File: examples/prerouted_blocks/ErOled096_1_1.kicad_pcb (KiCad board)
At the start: 2 copper layers, 9 parts

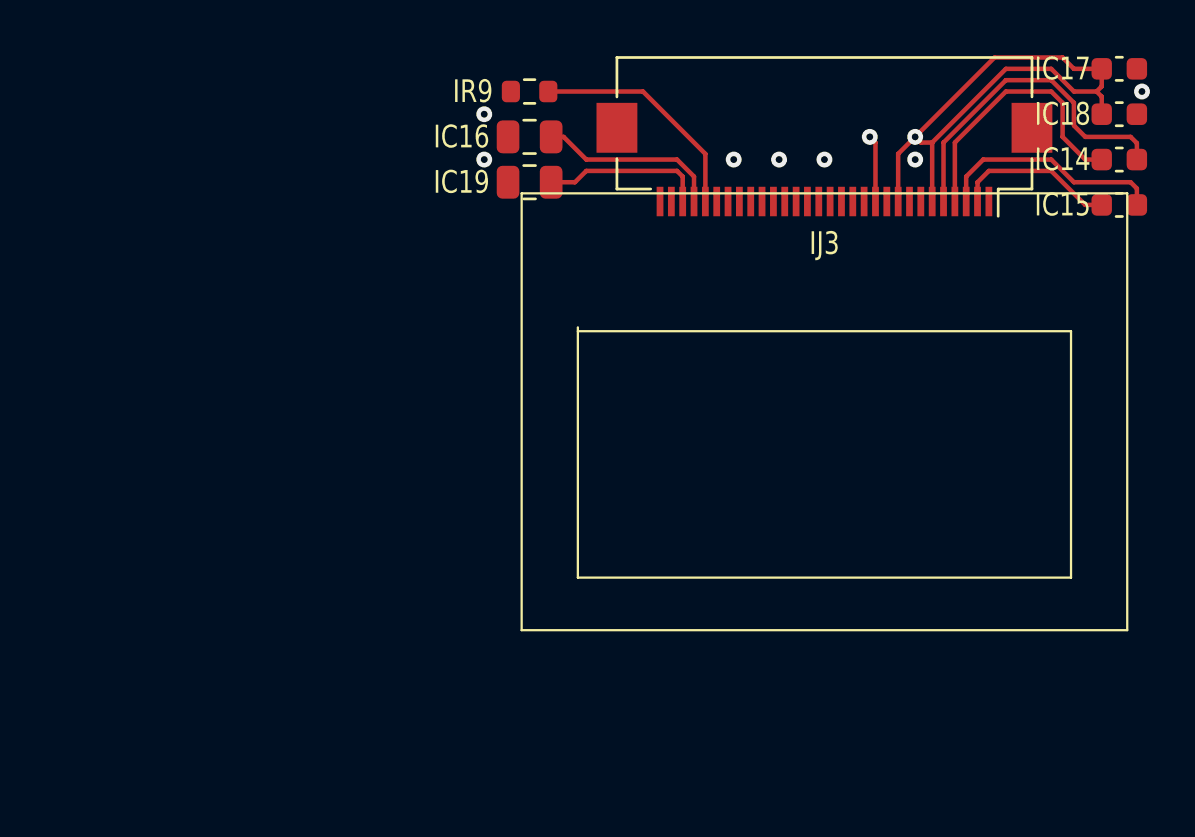
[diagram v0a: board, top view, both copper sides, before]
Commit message: Pcbbot (#314)
Robot driver that uses a ESP32 w/ camera and has student-proofing
  Key features:
  - USB-C receptacle for power input and battery charging.
- LiPo battery connector with voltage regulation and protection
circuits.
- Power management with priority power selection, fuse protection, and
gate control.
  - 3.3V voltage regulation for the main logic level power supply.
  - Integrated battery charging circuit with status indication.
  - I2C communication interface with pull-up resistors and test points.
  - Time-of-flight (ToF) sensor array for distance measurement.
- Inertial Measurement Unit (IMU) and magnetometer for orientation
sensing.
  - IO expander for additional GPIOs and a thru-hole RGB LED indicator.
  - OLED display
  - PWM Servo motor
  - Neopixel LED array for RGB lighting
  - Camera module with voltage regulation for image capture.
  - Digital switch for power control.
  - Keyboard mechanical switch with RGB LED
  - Ducky touch button
  
  Known issues:
  - Charging ic is not reverse protected
- MCU does not get turned off with the gate when powered by the USB and
battery, though the vbatt line turns off. (by design)

---------

Co-authored-by: Richard Lin <richard.lin@berkeley.edu>
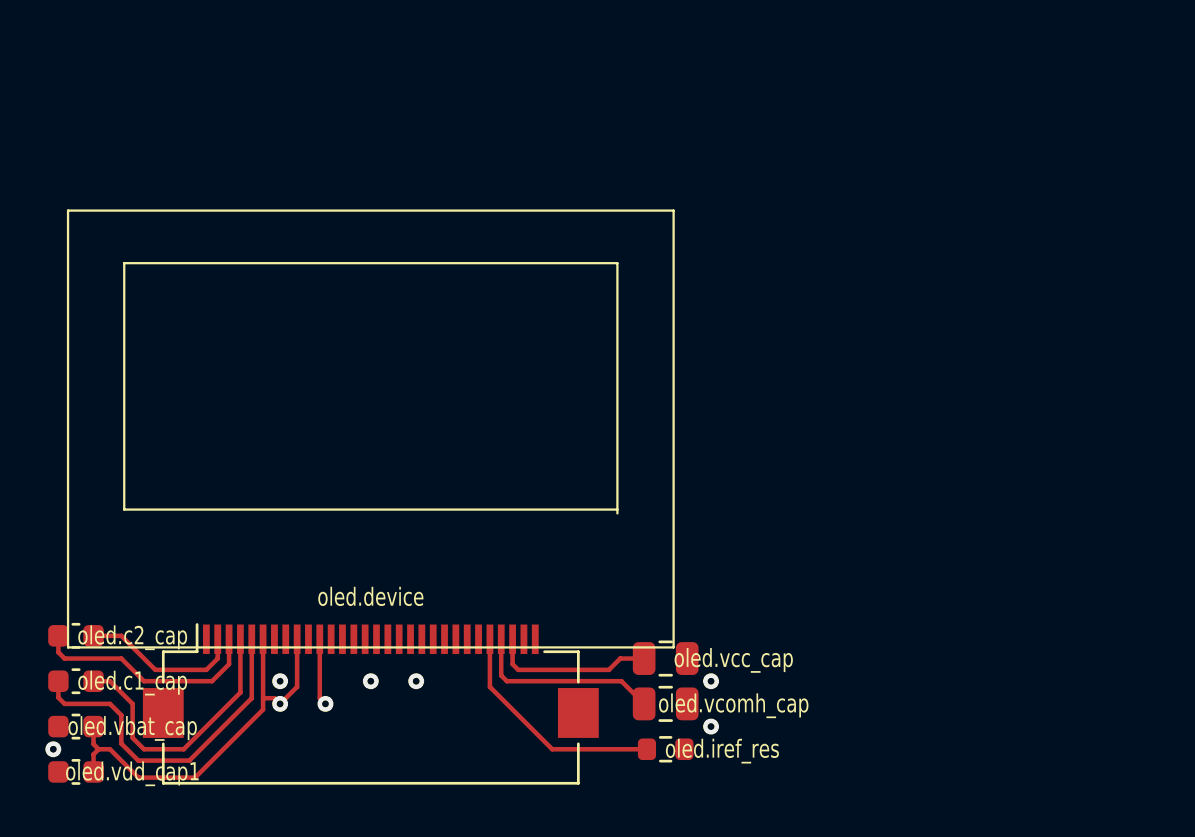
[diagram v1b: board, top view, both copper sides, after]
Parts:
- removed IC14, IC15, IC17, IC18: , Capacitor_SMD:C_0603_1608Metric
- removed IC16, IC19: , Capacitor_SMD:C_0805_2012Metric
- removed IJ3: AFC01-S30FCA-00 (Jushuo), Connector_FFC-FPC:Hirose_FH12-30S-0.5SH_1x30-1MP_P0.50mm_Horizontal
- removed IR9: , Resistor_SMD:R_0603_1608Metric
- removed IU7: ER-OLED-0.96-1.1 (EastRising), edg:Lcd_Er_Oled0.96_1.1_Outline
- added oled.c1_cap: , Capacitor_SMD:C_0603_1608Metric, F.Cu at (137.0, 133.0)
- added oled.c2_cap: , Capacitor_SMD:C_0603_1608Metric, F.Cu at (137.0, 131.0)
- added oled.device: AFC01-S30FCA-00, Connector_FFC-FPC:Hirose_FH12-30S-0.5SH_1x30-1MP_P0.50mm_Horizontal, F.Cu at (150.0, 133.0)
- added oled.iref_res: , Resistor_SMD:R_0603_1608Metric, F.Cu at (163.0, 136.0)
- added oled.lcd: ER-OLED-0.96-1.1, edg:Lcd_Er_Oled0.96_1.1_Outline, F.Cu at (150.0, 120.0)
- added oled.vbat_cap: , Capacitor_SMD:C_0603_1608Metric, F.Cu at (137.0, 135.0)
- added oled.vcc_cap: , Capacitor_SMD:C_0805_2012Metric, F.Cu at (163.0, 132.0)
- added oled.vcomh_cap: , Capacitor_SMD:C_0805_2012Metric, F.Cu at (163.0, 134.0)
- added oled.vdd_cap1: , Capacitor_SMD:C_0603_1608Metric, F.Cu at (137.0, 137.0)
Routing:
- net Iv3v3: track 30.6 -> 0.00 mm, vias 2 -> 0
- net v3v3: track 0.00 -> 21.3 mm, vias 0 -> 2
- net oled.c1_cap.neg: track 0.00 -> 14.9 mm
- net Ioled.c1_cap.neg: track 14.7 -> 0.00 mm
- net Ioled.c1_cap.pos: track 12.1 -> 0.00 mm
- net oled.c1_cap.pos: track 0.00 -> 12.0 mm
- net oled.c2_cap.neg: track 0.00 -> 10.2 mm
- net Ioled.c2_cap.neg: track 10.2 -> 0.00 mm
- net oled.iref_res.a: track 0.00 -> 10.2 mm
- net Ioled.iref_res.a: track 10.2 -> 0.00 mm
- net oled.device.vcomh: track 0.00 -> 8.42 mm
- net Ioled.device.vcomh: track 8.12 -> 0.00 mm
- net Ioled.device.vcc: track 7.21 -> 0.00 mm
- net oled.device.vcc: track 0.00 -> 7.21 mm
- net oled.c2_cap.pos: track 0.00 -> 7.15 mm
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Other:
- copper layers 2 -> 4
